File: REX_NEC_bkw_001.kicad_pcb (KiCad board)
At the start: 2 copper layers, 16.3 x 34 mm, 9 parts, among them J1 DIP28 legs 27C256, J2 JTAG, J3 PRG, U1 XCR3064-VQ44, U2 29F800, U3 LP2980

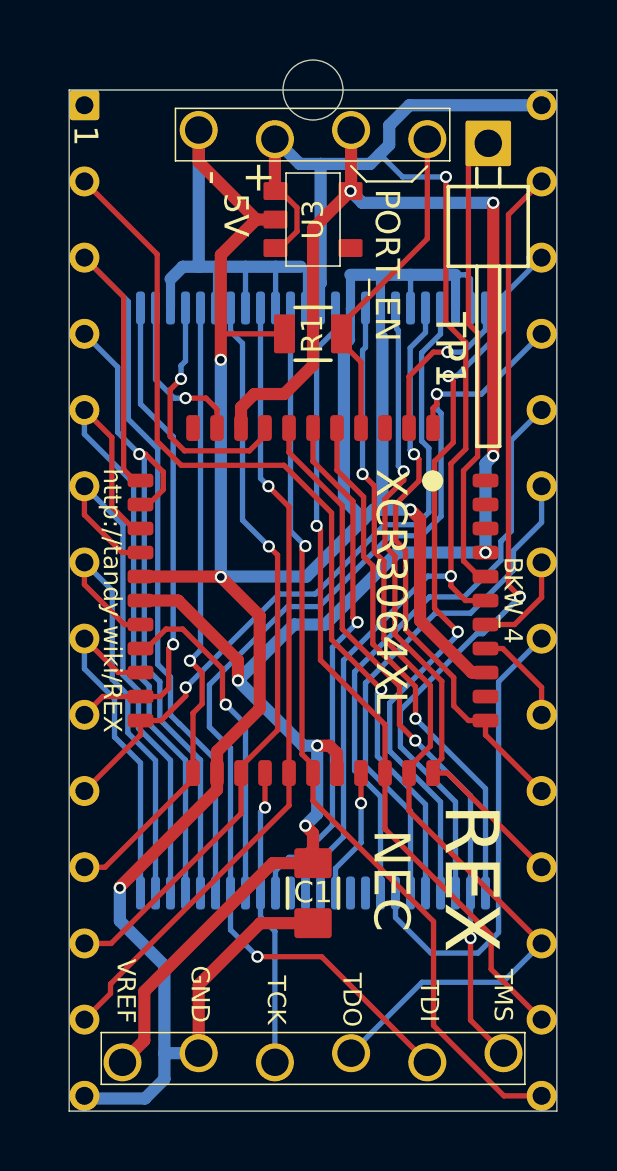
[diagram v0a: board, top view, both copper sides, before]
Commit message: upgrade board outline and carrier to v004
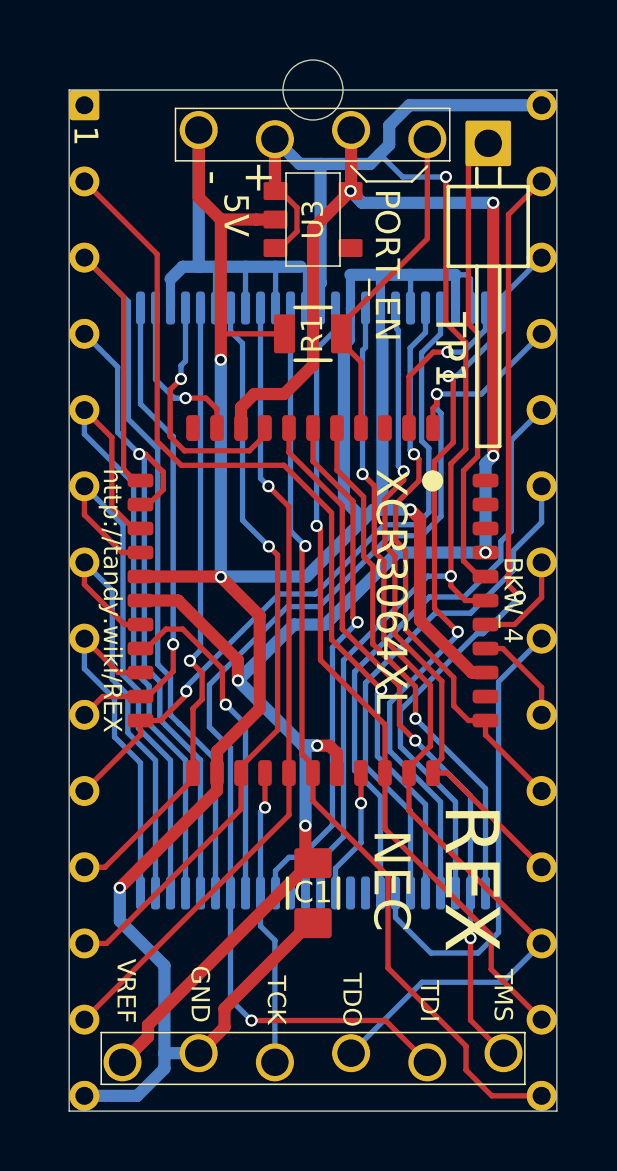
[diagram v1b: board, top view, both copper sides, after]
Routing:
- net /eA8: track 36.5 -> 37.9 mm
- net GND: track 106.9 -> 105.9 mm
- net +3V3: track 62.7 -> 62.2 mm
